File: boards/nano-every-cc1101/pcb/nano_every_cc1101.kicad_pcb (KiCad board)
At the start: 2 copper layers, 100 x 100 mm, 84 parts, among them J1 SMA, J2 SMA, J3 Breakout 1-15, J4 Breakout 16-30, U1 CC1101RGPR, U2 AP2112K-3.3, U3 TXS0108EPWR, U501 CC1101RGPR, Y1 26MHz, Y501 26MHz

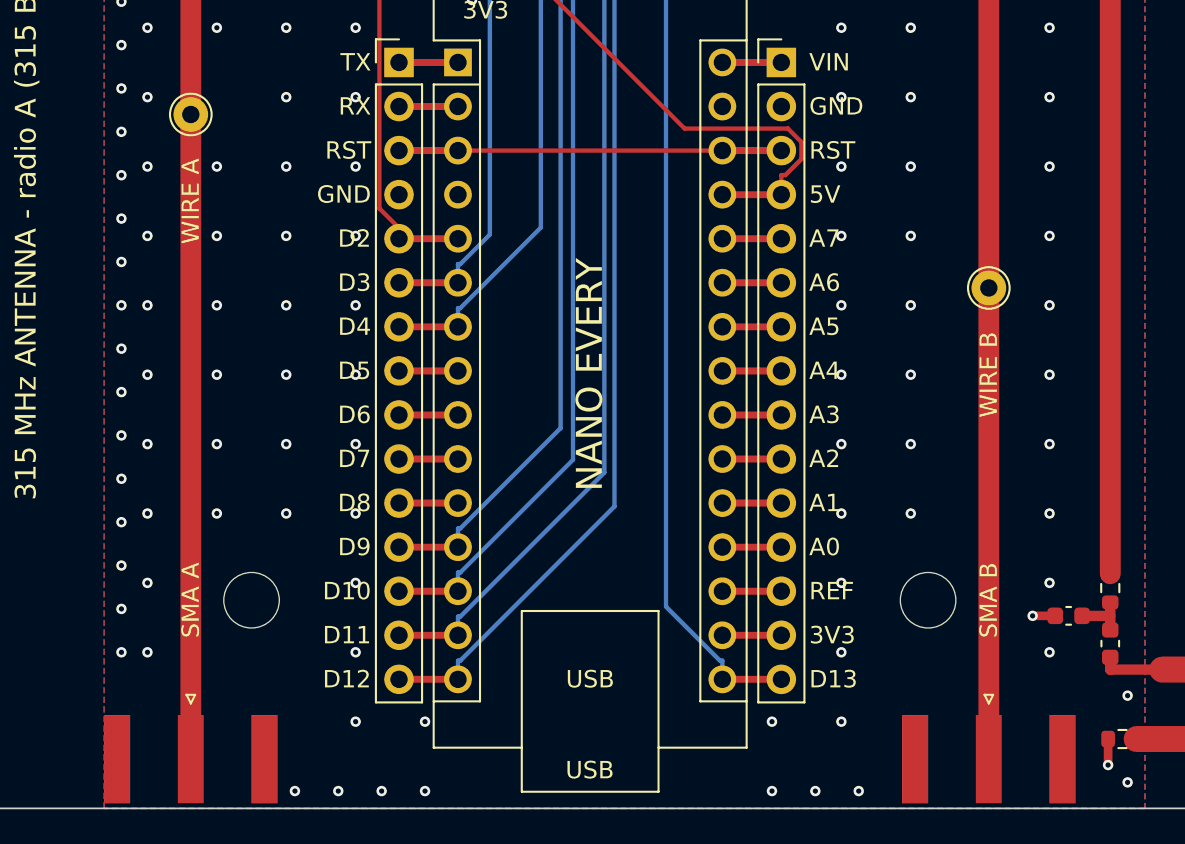
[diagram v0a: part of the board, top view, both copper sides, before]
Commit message: nano-every-cc1101: JLCPCB-stocked SMA jacks (C496550), J3/J4 headers in the assembly BOM/CPL
J1/J2 move to the BAT WIRELESS BWSMA-KE-P001 edge-mount jack with a local
footprint from its LCSC land pattern (ground legs at +/-2.55 mm). The
routing is otherwise unchanged. J3/J4 get LCSC C7501269 and are placed by
their centre in the CPL.

Co-Authored-By: Claude Opus 5.5 <noreply@anthropic.com>
Claude-Session: https://claude.ai/code/session_019aUkwoH7eUuCGWSrK9KSBc
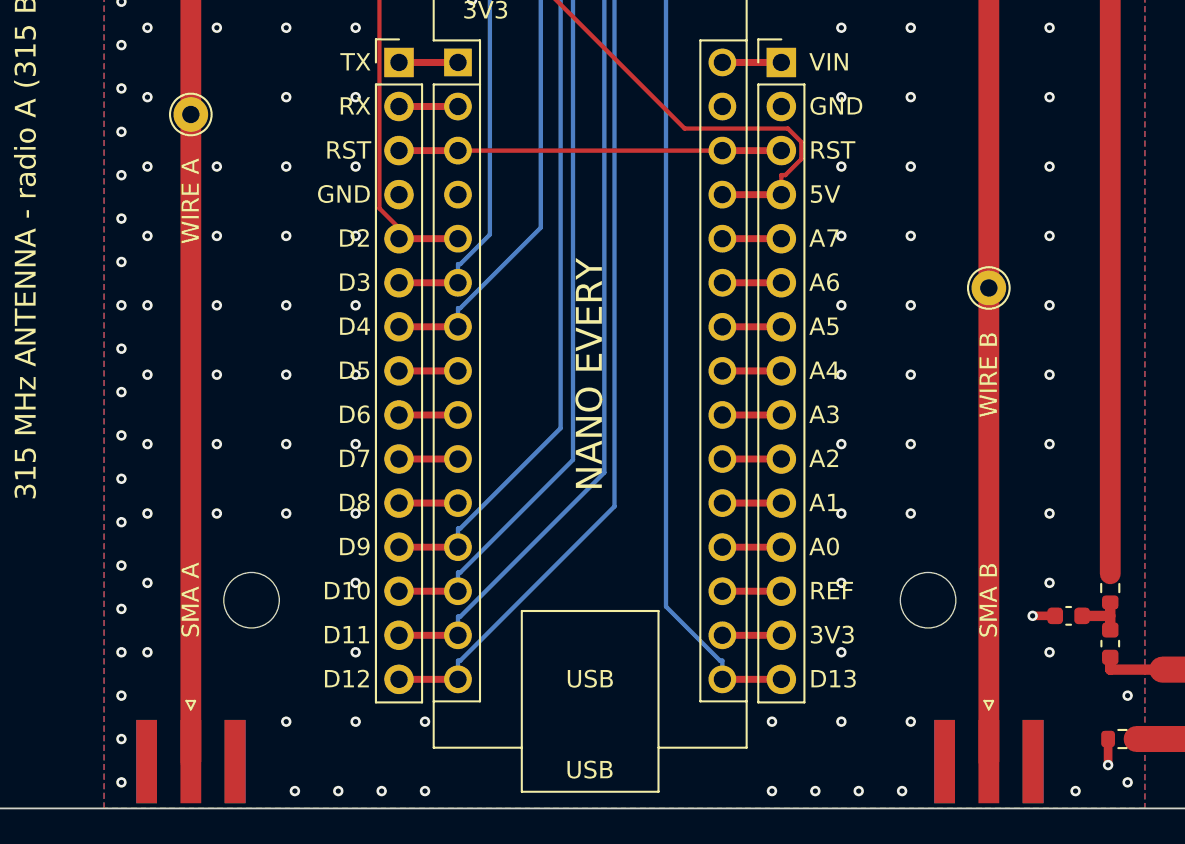
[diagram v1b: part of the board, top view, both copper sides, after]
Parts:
- J1, J2: footprint Connector_Coaxial:SMA_Amphenol_132289_EdgeMount -> nano_every_cc1101:SMA_BWSMA-KE-P001_EdgeMount
- moved J1 0.14 mm to (127.0, 197.3)
- moved J2 0.14 mm to (173.0, 197.3)
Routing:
- net GND: vias 223 -> 230

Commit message: nano-every-cc1101: JLCPCB basic/preferred parts wherever electrically equivalent
100 nF, 27/100/12 pF 0402, 10 pF 0603 and 56k now use JLCPCB basic or
preferred-extended parts (no loading fee). C124/C125 (DC block / RF bypass)
go 220 -> 330 pF C0G and the power LED goes red, the fee-free options for
those positions. RF match values, RF inductors and ICs have no fee-free
equivalent and stay as they are. Board geometry and Gerbers unchanged.

Co-Authored-By: Claude Opus 5.5 <noreply@anthropic.com>
Claude-Session: https://claude.ai/code/session_019aUkwoH7eUuCGWSrK9KSBc
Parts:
- C124, C125: value 220pF -> 330pF
- D1: value green -> red

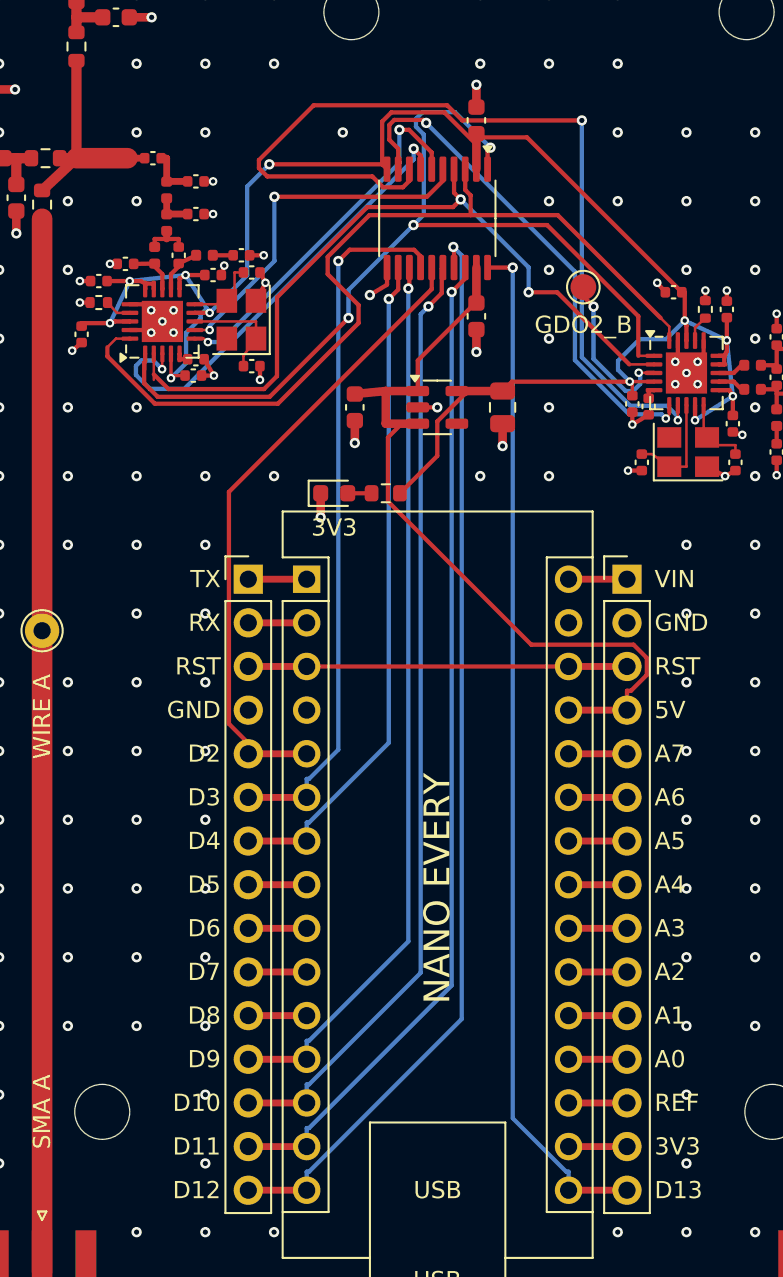
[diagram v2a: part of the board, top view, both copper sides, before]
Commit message: nano-every-cc1101: minimum-cost BOM, 13 extended part types left
- Antenna T-match / tuning defaults re-optimised over JLCPCB basic and
  preferred 0603 values only (tune.py CHEAP_CAPS); the 315 MHz arm keeps
  the 39 nH wire-wound, the fee-free 68 nH multilayer is too lossy there.
  All four defaults still cover their ISM bands (S11 -15.6 to -35.6 dB).
- 3.3 V LDO: AP2112K (SOT-23-5) -> XC6206P332MR (SOT-23, basic part),
  ground tied to C6's pad so the autorouter still closes every net.
- 868/915 balun 1.0/1.5/3.3 pF -> fee-free +/-0.25 pF parts.
DRC: 0 unconnected, 14 cosmetic items.

Co-Authored-By: Claude Opus 5.5 <noreply@anthropic.com>
Claude-Session: https://claude.ai/code/session_019aUkwoH7eUuCGWSrK9KSBc
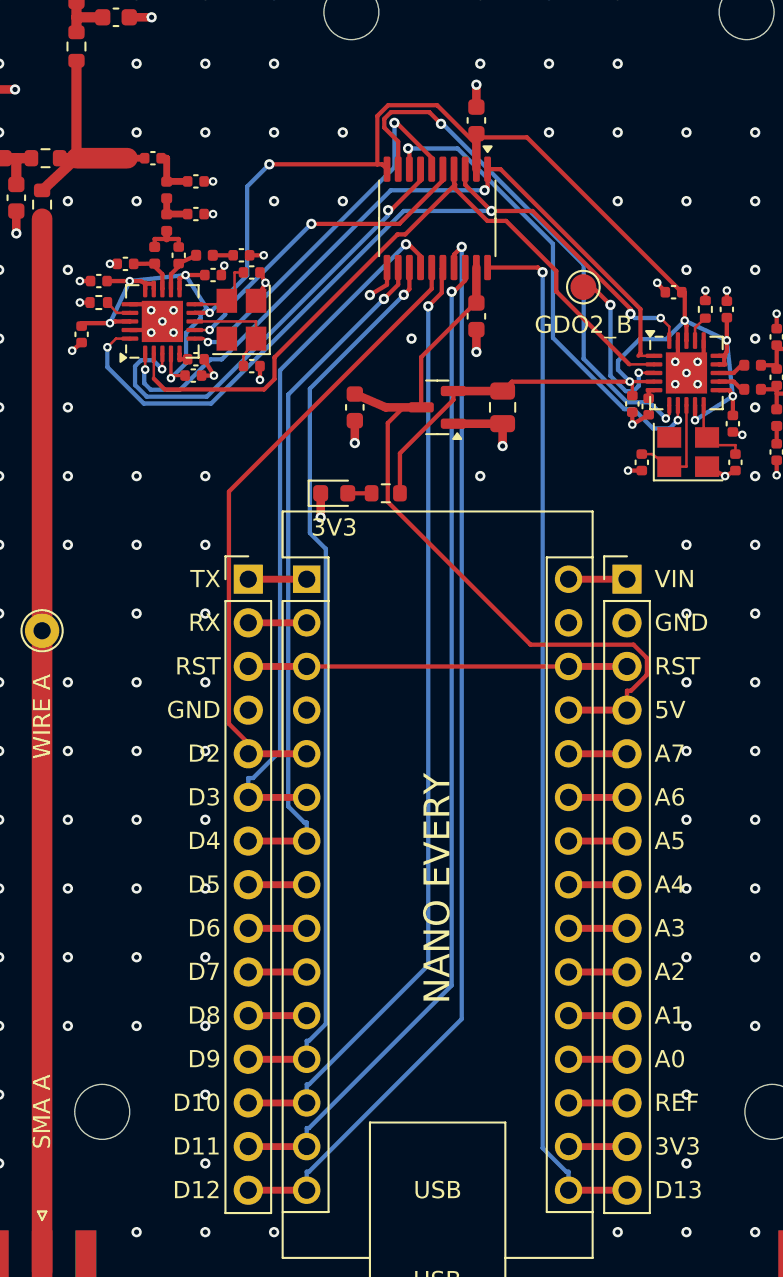
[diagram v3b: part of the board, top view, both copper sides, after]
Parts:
- C301: value 1.1pF -> 3pF
- C311: value 10pF -> 47pF
- C321: value 3.6pF -> 3pF
- C331, L331: value 2.7pF -> 3pF
- L301: value 5.1pF -> 6pF
- L311: value 0R -> 18pF
- L321: value 6.2pF -> 6pF
- L401: value 51pF -> 47pF
- R311: value DNP (2.7pF to use) -> DNP (0R to use)
- U2: value AP2112K-3.3 -> XC6206P332MR; footprint Package_TO_SOT_SMD:SOT-23-5 -> Package_TO_SOT_SMD:SOT-23
- turned U2 to 180 degrees
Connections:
- U2 pad 1: +5V -> GND
- U2 pad 2: GND -> 3V3
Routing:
- net CSN_B: track 52.9 -> 28.0 mm
- net SCLK: track 55.1 -> 43.8 mm, vias 3 -> 2
- net SI: track 51.5 -> 47.7 mm, vias 0 -> 4
- net SO: track 45.1 -> 42.7 mm, vias 2 -> 0
- net CSN_A: track 21.0 -> 18.8 mm
- net GND: track 43.0 -> 44.7 mm, vias 230 -> 227
- net +5V: track 46.8 -> 45.3 mm
- net GDO0_B: track 30.1 -> 31.2 mm
- net D4: track 39.1 -> 40.0 mm
- net D13_SCK: track 60.0 -> 60.8 mm
- net D9: track 52.0 -> 52.8 mm
- net 3V3: track 113.3 -> 114.0 mm
- net GDO0_A: track 21.6 -> 22.2 mm

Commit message: nano-every-cc1101: leave optional parts out of assembly (10 extended types)
SMA jacks J1/J2, breakout headers J3/J4 and the 315 MHz antenna's 39 nH
arm inductor L402 stay on the board as footprints but are hand-fit
options, so the JLCPCB order has no through-hole step (Economic PCBA)
and three fewer extended part types. Board copper and Gerbers unchanged.

Co-Authored-By: Claude Opus 5.5 <noreply@anthropic.com>
Claude-Session: https://claude.ai/code/session_019aUkwoH7eUuCGWSrK9KSBc
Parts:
- L402: value 39nH -> DNP (39nH to use)

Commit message: nano-every-cc1101: coil (helical spring) antenna positions H1/H2
H1/H2 become 1.2 mm coil-antenna holes (BAT WIRELESS BWxxxSNX spring
antennas, 315/433/868/915 MHz, LCSC C496553-C496556) selected by
R403/R406 as before. New DNP links R407/R408 cut the line on to the SMA
jacks so a fitted coil sees no 30-40 mm open stub; fit them 0R to use the
SMA. Coils listed as optional hand-fit parts in the purchasing BOM.
DRC: 0 unconnected, same 14 cosmetic items.

Co-Authored-By: Claude Opus 5.5 <noreply@anthropic.com>
Claude-Session: https://claude.ai/code/session_019aUkwoH7eUuCGWSrK9KSBc
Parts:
- added R407: DNP, Resistor_SMD:R_0603_1608Metric, F.Cu at (127.0, 164.5)
- added R408: DNP, Resistor_SMD:R_0603_1608Metric, F.Cu at (173.0, 174.5)
- H1, H2: value wire -> coil; footprint TestPoint:TestPoint_THTPad_D2.0mm_Drill1.0mm -> TestPoint:TestPoint_THTPad_D2.5mm_Drill1.2mm
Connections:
- J1 pad 1: EXT_A -> SMA_A
- J2 pad 1: EXT_B -> SMA_B
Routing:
- net EXT_A: track 61.3 -> 27.7 mm
- net SMA_A: track 0.00 -> 32.0 mm
- net EXT_B: track 51.3 -> 27.7 mm
- net SMA_B: track 0.00 -> 22.0 mm
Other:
- board text added: "COIL A"
- board text added: "COIL B"
- board text added: "coil in H1/H2: BAT WIRELESS BWxxxSNX spring"
- board text added: "radio A: 433 R301 | 315 R311 | coil R403 | SMA +R407"
- board text added: "radio B: 868 R321 | 915 R331 | coil R406 | SMA +R408"
- board text removed: "WIRE A"
- board text removed: "WIRE B"
- board text removed: "radio A: 433 R301 | 315 R311 | SMA/wire R403"
- board text removed: "radio B: 868 R321 | 915 R331 | SMA/wire R406"
- board text removed: "whip for SMA/wire: L(mm) = 71250 / f(MHz)"
